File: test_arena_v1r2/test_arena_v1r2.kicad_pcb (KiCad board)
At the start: 4 copper layers, 105 x 50 mm, 48 parts, among them J1 Conn_01x05_Socket, J2 Conn_01x05_Socket, J3 Barrel_Jack, U1 Teensy4.1, U2 SN74LV1T34DBV, U3 74LVC2G17, U4 74LVC2G17, U5 74LVC2G17, U6 74LVC2G17

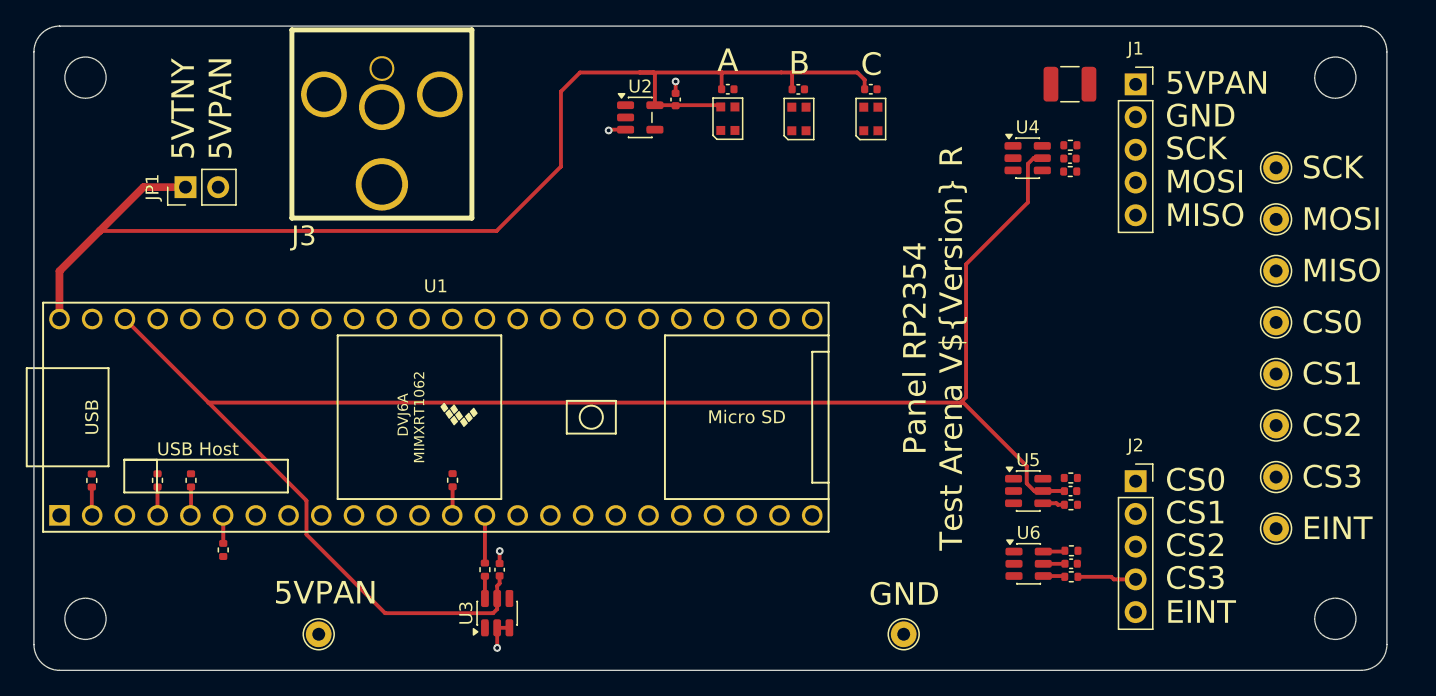
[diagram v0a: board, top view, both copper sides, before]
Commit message: Added final design for modified test arena.
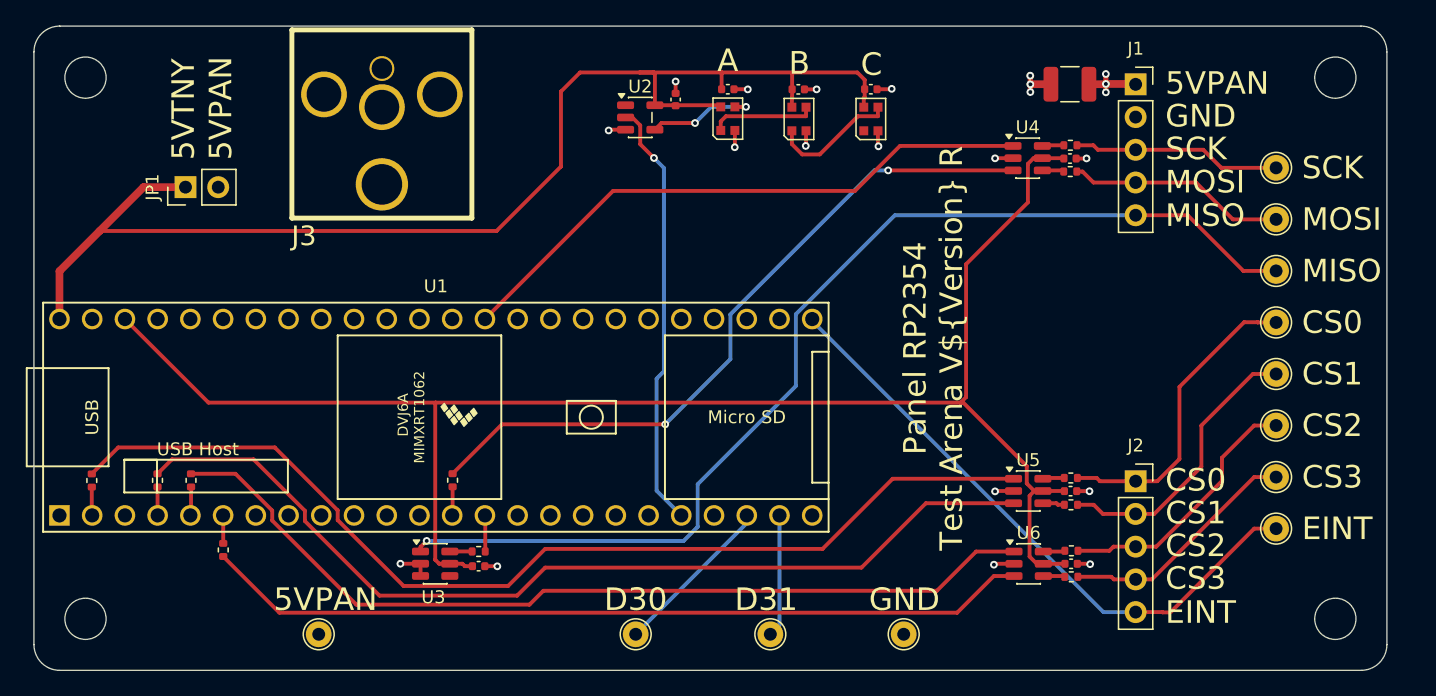
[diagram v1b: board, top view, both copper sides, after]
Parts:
- added TP11: TestPoint, TestPoint:TestPoint_THTPad_D2.0mm_Drill1.0mm, F.Cu at (96.7, 97.2)
- added TP12: TestPoint, TestPoint:TestPoint_THTPad_D2.0mm_Drill1.0mm, F.Cu at (107.2, 97.2)
- moved U3 6.16 mm to (81.1, 91.7), turned to 0 degrees
- moved C5 1.65 mm to (84.5, 91.9), turned to 0 degrees
- moved R6 1.49 mm to (84.5, 90.8), turned to 0 degrees
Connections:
- U1 pad 22: unconnected-(U1-30_CRX3-Pad22) -> /D30
- U1 pad 23: unconnected-(U1-31_CTX3-Pad23) -> /D31
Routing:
- net /MISO: track 0.00 -> 84.4 mm, vias 0 -> 1
- net /CS0: track 0.00 -> 80.7 mm
- net /CS1: track 0.00 -> 74.7 mm
- net /CS2: track 0.00 -> 70.2 mm
- net /CS3: track 0.00 -> 64.4 mm
- net /MOSI: track 0.00 -> 55.3 mm, vias 0 -> 2
- net /EINT: track 0.00 -> 48.2 mm
- net /SCK: track 0.00 -> 46.5 mm
- net /DLED: track 0.00 -> 33.5 mm, vias 0 -> 1
- net /CS0_PAN: track 0.00 -> 23.9 mm
- net /CS1_PAN: track 0.00 -> 22.1 mm
- net /CS2_PAN: track 0.00 -> 20.5 mm
- net /MOSI_PAN: track 0.00 -> 17.0 mm
- net GND: track 5.74 -> 22.7 mm, vias 4 -> 19
- net /SCK_PAN: track 0.00 -> 16.2 mm
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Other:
- board text added: "D30"
- board text added: "D31"
